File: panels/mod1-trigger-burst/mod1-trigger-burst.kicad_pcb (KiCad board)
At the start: 2 copper layers, 19.8 x 128.5 mm, 0 parts

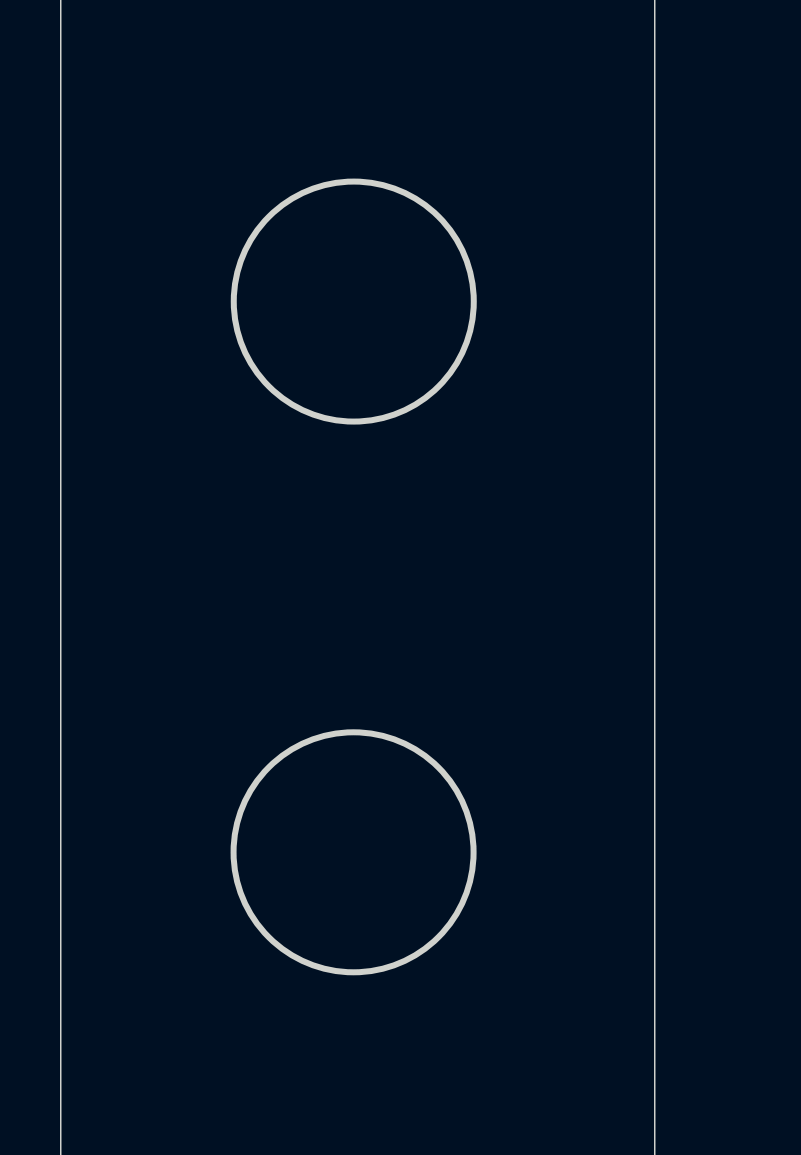
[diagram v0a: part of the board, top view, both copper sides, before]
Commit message: move vcvrack, update faceplates
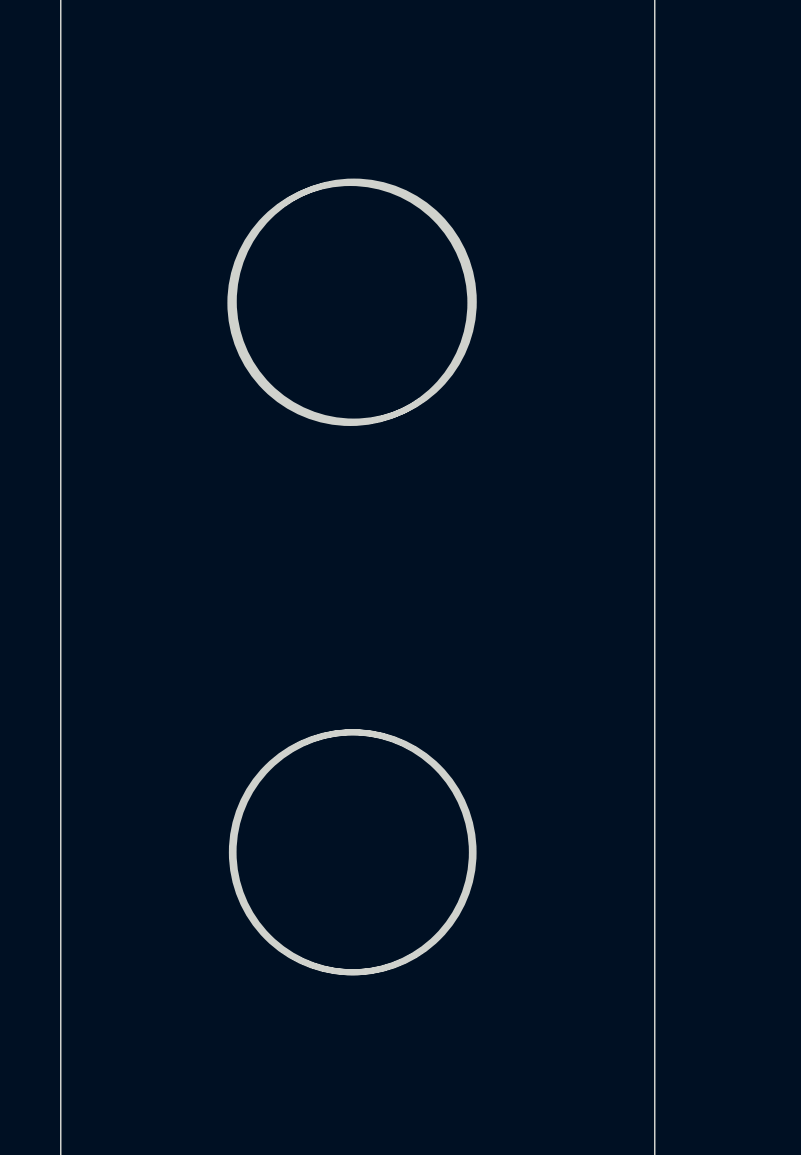
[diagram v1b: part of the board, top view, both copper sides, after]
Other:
- outline, holes or cut-outs redrawn
- board text added: "/16"
- board text added: "/2"
- board text added: "/3"
- board text added: "/4"
- board text added: "/6"
- board text added: "/8"
- board text added: "1"
- board text added: "16"
- board text added: "3"
- board text added: "4"
- board text added: "6"
- board text added: "8"
- board text added: "Burst"
- board text added: "Division"
- board text added: "Out"
- board text added: "TRIG BURST"
- board text added: "output"
- board text added: "trigger"
- board text removed: "BURST"
- board text removed: "Div"
- board text removed: "Num"
- board text removed: "NumCV"
- board text removed: "trig"
